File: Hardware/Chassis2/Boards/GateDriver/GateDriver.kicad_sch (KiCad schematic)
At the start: 23 parts, among them J1 Conn_02x08_Counter_Clockwise

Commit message: New gate driver
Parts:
- removed H4, H5: MountingHole_Pad, MountingHole:MountingHole_2.2mm_M2_Pad, symbol Mechanical:MountingHole_Pad
- removed Q1: ~, InverterCom:62mm_power_module, symbol InverterCom:62mm_power_module
- removed R1, R2, R3, R4, R5, R6: 4.7k, Resistor_SMD:R_1210_3225Metric_Pad1.30x2.65mm_HandSolder, symbol Device:R
- removed TP5, TP6: TestPoint, TestPoint:TestPoint_Loop_D2.54mm_Drill1.5mm_Beaded, symbol Connector:TestPoint
- added H2, H4, H5, H6, H7, H8: MountingHole, MountingHole:MountingHole_5.3mm_M5_ISO7380_Pad, symbol Mechanical:MountingHole
- added J2, J3, J4: TBP01R2W-508-06BE, SHDR6W100P0X508_1X6_4064X850X1240P, symbol InverterCom:TBP01R2W-508-06BE
- H1, H3: footprint MountingHole:MountingHole_3.2mm_M3 -> MountingHole:MountingHole_5.3mm_M5_ISO7380_Pad
- renumbered C3 to C1, LED5 to LED1, R17 to R1, R8 to R2, TP3 to TP1, TP1 to TP2, TP2 to TP3
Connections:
- net PH_L is gone; now on net GND_A: J1.10 (Pin_10)
- net GND_A: no longer J1.11 (Pin_11), J1.3 (Pin_3), J1.5 (Pin_5), J1.7 (Pin_7), J1.8 (Pin_8)
- net READY: now also J1.3 (Pin_3); no longer J1.4 (Pin_4)
- net RESET: now also J1.4 (Pin_4); no longer J1.6 (Pin_6)
- net PH_H renamed PH_W_H
- new net PH_U_H: J1.6 (Pin_6)
- new net PH_U_H_C: J2.6
- new net PH_U_H_E: J2.4
- new net PH_U_H_G: J2.5
- new net PH_U_L: J1.5 (Pin_5)
- new net PH_U_L_C: J2.3
- new net PH_U_L_E: J2.1
- new net PH_U_L_G: J2.2
- new net PH_V_H: J1.8 (Pin_8)
- new net PH_V_H_C: J3.6
- new net PH_V_H_E: J3.4
- new net PH_V_H_G: J3.5
- new net PH_V_L: J1.7 (Pin_7)
- new net PH_V_L_C: J3.3
- new net PH_V_L_E: J3.1
- new net PH_V_L_G: J3.2
- new net PH_W_H_C: J4.6
- new net PH_W_H_E: J4.4
- new net PH_W_H_G: J4.5
- new net PH_W_L: J1.11 (Pin_11)
- new net PH_W_L_C: J4.3
- new net PH_W_L_E: J4.1
- new net PH_W_L_G: J4.2
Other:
- added sheet SingleChannelDriver2 (SingleChannelDriver.kicad_sch)
- added sheet SingleChannelDriver3 (SingleChannelDriver.kicad_sch)
- added sheet SingleChannelDriver4 (SingleChannelDriver.kicad_sch)
- added sheet SingleChannelDriver5 (SingleChannelDriver.kicad_sch)
- note removed: "(DC LINK +)"
- note removed: "(PHASE LEG)"
- note removed: "Pull up to make FAULT pin readable."
- note removed: "Pull up to make READY pin readable."
- note removed: "Pull up to make RPI manually clear fault."
- note removed: "READY IS ACTIVE HIGH, READY SHOULD BE HIGH DURING NORMAL OPERATION"
- note removed: "RESET IS ACTIVE LOW, WE PULL UP TO MAKE IT REQUIRE MCU INTERVENTION"
- note removed: "WE ARE EXPECTING FAULT TO BE ACTIVE LOW READING FAULT AS NOT HIGH INDICATES ISSUE"
- note removed: "maybe check that these resistors default to safe state"
- moved on the sheet: C1, J1, LED1, LED2, R1, R2, TP1, TP2, TP3, TP4

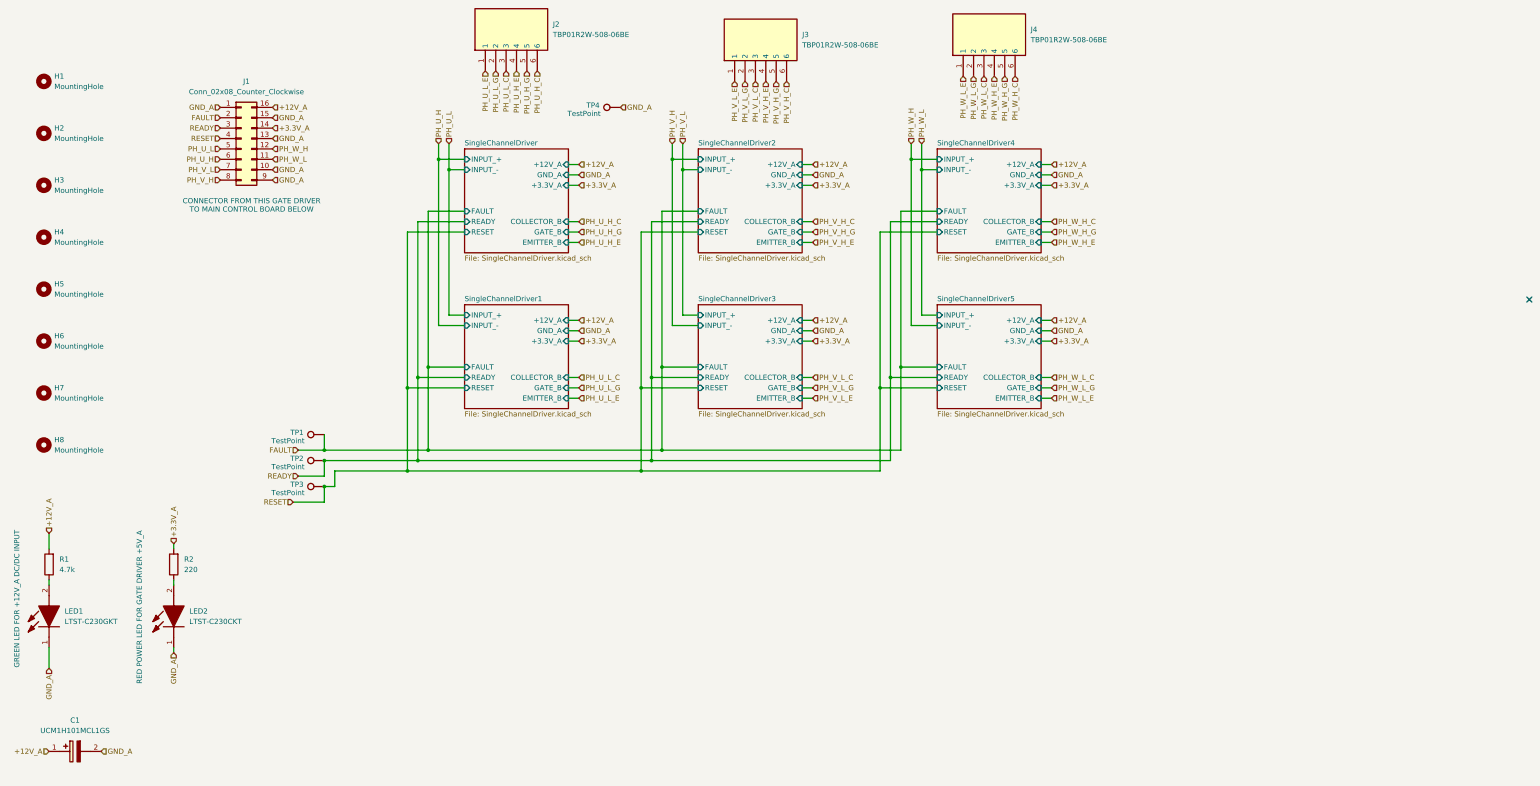
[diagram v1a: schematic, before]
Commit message: Finish gate driver board
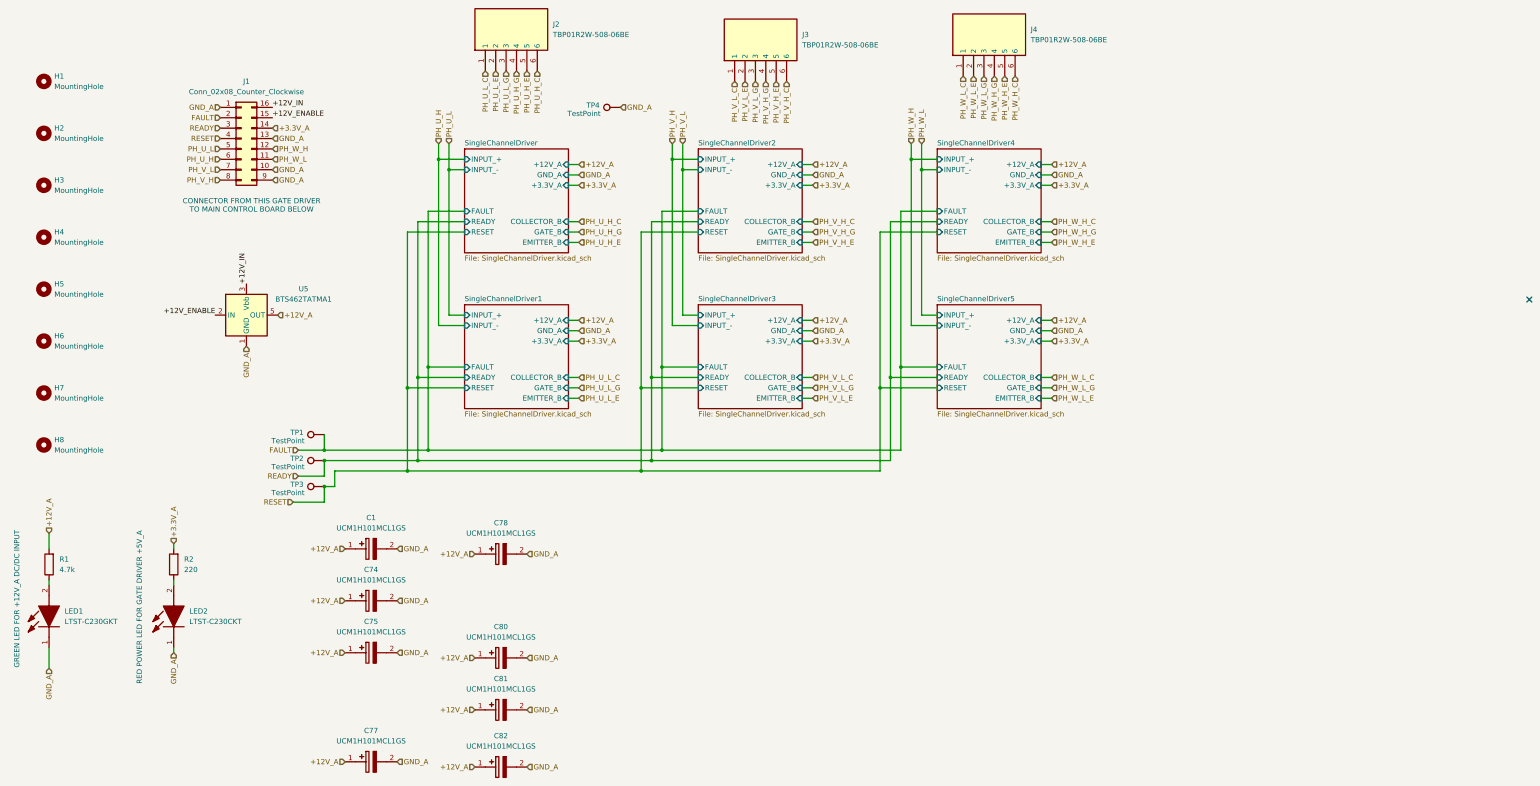
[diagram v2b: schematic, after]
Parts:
- added C74, C75, C77, C78, C80, C81, C82: UCM1H101MCL1GS, CAPAE660X800N, symbol InverterCom:UCM1H101MCL1GS
- added U5: BTS462TATMA1, Package_TO_SOT_SMD:TO-252-4, symbol Power_Management:BTS462TATMA1
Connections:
- net +12V_A: now also C74.1 (+), C75.1 (+), C77.1 (+), C78.1 (+), C80.1 (+), C81.1 (+), C82.1 (+), U5.5 (OUT); no longer J1.16 (Pin_16)
- net GND_A: now also C74.2 (-), C75.2 (-), C77.2 (-), C78.2 (-), C80.2 (-), C81.2 (-), C82.2 (-), U5.1 (GND); no longer J1.15 (Pin_15)
- net PH_U_H_E: now also J2.5; no longer J2.4
- net PH_U_H_G: now also J2.4; no longer J2.5
- net PH_U_L_C: now also J2.1; no longer J2.3
- net PH_U_L_E: now also J2.2; no longer J2.1
- net PH_U_L_G: now also J2.3; no longer J2.2
- net PH_V_H_E: now also J3.5; no longer J3.4
- net PH_V_H_G: now also J3.4; no longer J3.5
- net PH_V_L_C: now also J3.1; no longer J3.3
- net PH_V_L_E: now also J3.2; no longer J3.1
- net PH_V_L_G: now also J3.3; no longer J3.2
- net PH_W_H_E: now also J4.5; no longer J4.4
- net PH_W_H_G: now also J4.4; no longer J4.5
- net PH_W_L_C: now also J4.1; no longer J4.3
- net PH_W_L_E: now also J4.2; no longer J4.1
- net PH_W_L_G: now also J4.3; no longer J4.2
- new net +12V_ENABLE: J1.15 (Pin_15), U5.2 (IN)
- new net +12V_IN: J1.16 (Pin_16), U5.3 (Vbb)
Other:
- moved on the sheet: C1
